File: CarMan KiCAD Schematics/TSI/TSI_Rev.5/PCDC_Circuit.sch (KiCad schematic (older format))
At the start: 56 parts, among them IC1 TS431ILT, J30 GLV Hook-up Pin, K1 APAN3105, Q1 ZVP1320F, Q3 SI1302DL-T1-E3, U10 MC7805BDTRKG, U12 REF3033, U19 SN74HC00APWR, U21 MCP6004, U27 TLP293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

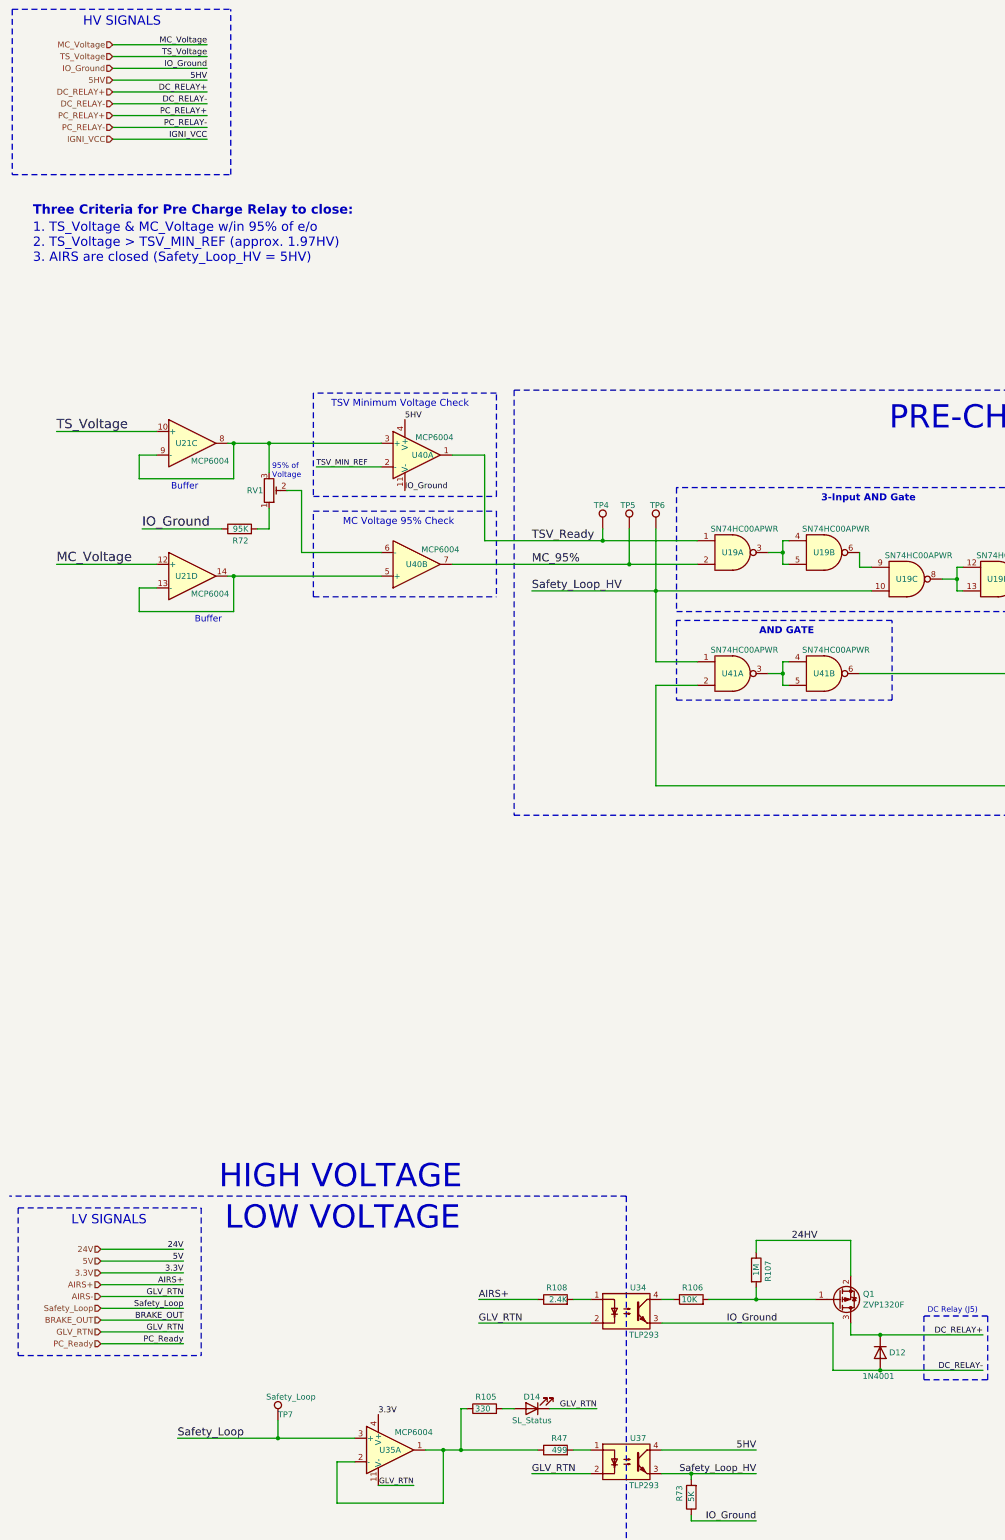
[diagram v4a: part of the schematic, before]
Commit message: General signal directions -> i/o
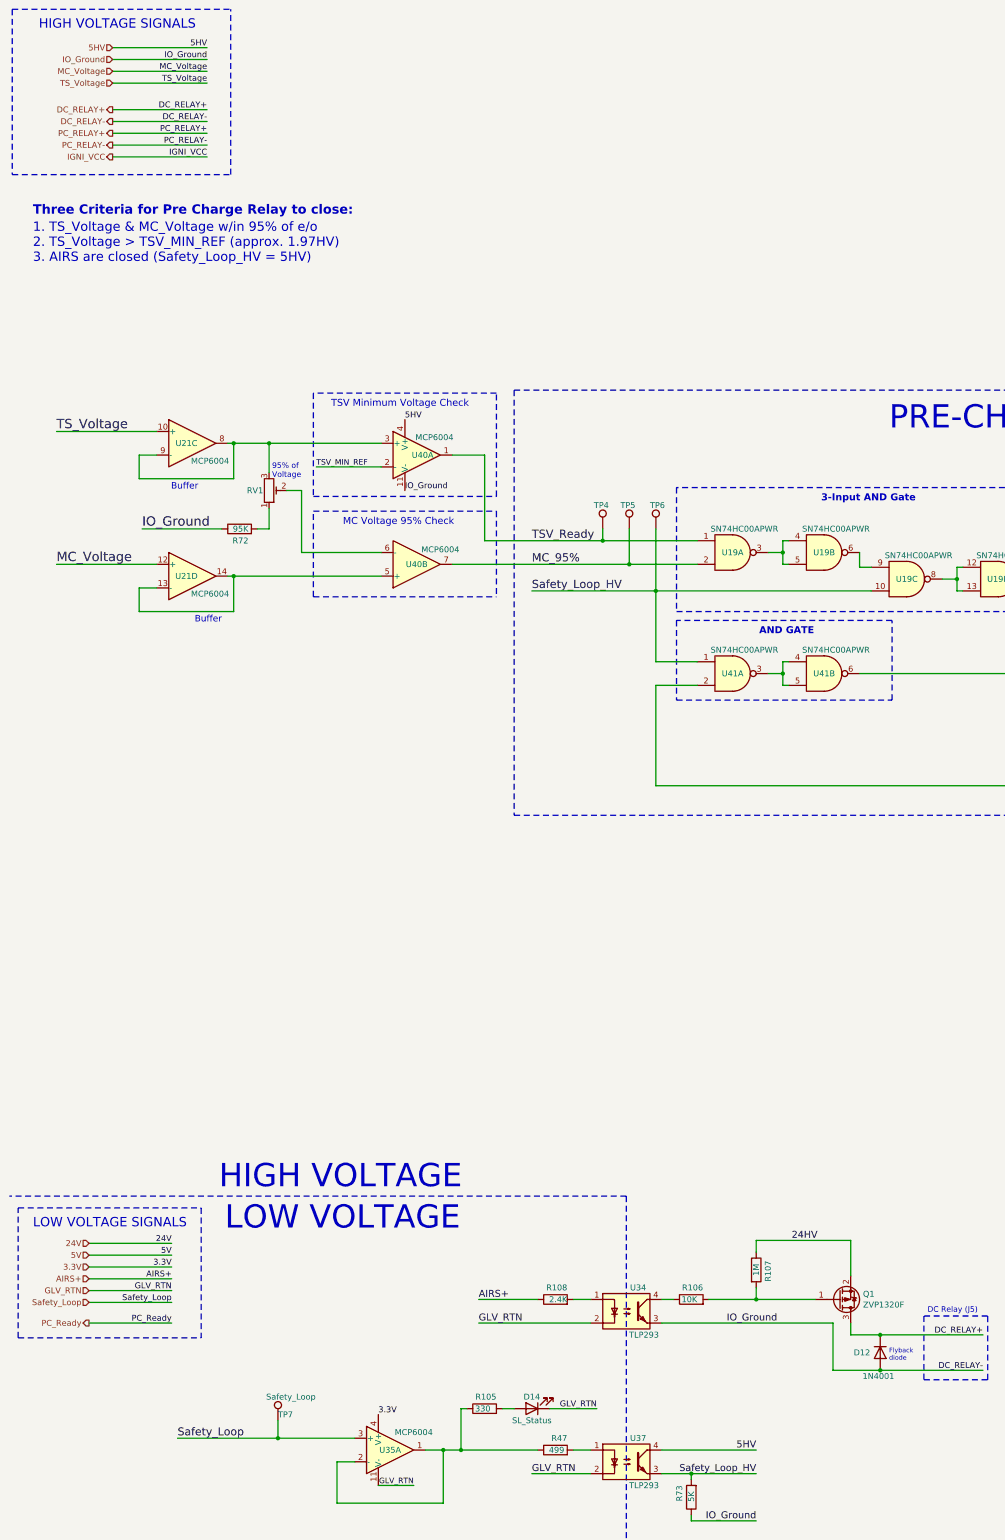
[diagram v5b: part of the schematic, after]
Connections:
- net AIRS- renamed GLV_RTN
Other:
- note added: "Flyback\ndiode"
- note added: "HIGH VOLTAGE SIGNALS\n"
- note added: "LOW VOLTAGE SIGNALS\n"
- note removed: "HV SIGNALS\n"
- note removed: "LV SIGNALS\n"
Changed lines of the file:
@@
 Text Label 21925 1850 2    47   ~ 0
 5HV
-Text Label 2150 800  2    50   ~ 0
+Text Label 2150 1025 2    50   ~ 0
 MC_Voltage
-Text Label 2150 1000 2    50   ~ 0
+Text Label 2150 925  2    50   ~ 0
 IO_Ground
-Text Label 2150 900  2    50   ~ 0
+Text Label 2150 1125 2    50   ~ 0
 TS_Voltage
-Text Notes 1100 650  0    79   ~ 0
-HV SIGNALS\n
-Text HLabel 1350 800  0    50   Input ~ 0
+Text Notes 725  675  0    79   ~ 0
+HIGH VOLTAGE SIGNALS\n
+Text HLabel 1350 1025 0    50   Input ~ 0
 MC_Voltage
 Text Notes 2300 10850 0    197  ~ 0
@@
 U 1 1 6017ACEB
 P 7850 11875
-F 0 "D12" V 7850 11950 50  0000 L CNN
+F 0 "D12" V 7850 11650 50  0000 L CNN
 F 1 "1N4001" V 8050 11725 50  0000 L CNN
 F 2 "Diode_THT:D_DO-41_SOD81_P7.62mm_Horizontal" H 7850 11875 50  0001 C CNN
@@
 Text Notes 13700 4125 0    79   ~ 0
 SR Latching Logic\n
-Text HLabel 1350 900  0    50   Input ~ 0
+Text HLabel 1350 1125 0    50   Input ~ 0
 TS_Voltage
-Text HLabel 1350 1000 0    50   Input ~ 0
+Text HLabel 1350 925  0    50   Input ~ 0
 IO_Ground
-Text Label 2150 1100 2    50   ~ 0
+Text Label 2150 825  2    50   ~ 0
 5HV
-Text HLabel 1350 1100 0    50   Input ~ 0
+Text HLabel 1350 825  0    50   Input ~ 0
 5HV
-Text Label 1950 11700 2    50   ~ 0
+Text Label 1850 11350 2    50   ~ 0
 GLV_RTN
-Text Label 1950 11000 2    50   ~ 0
+Text Label 1850 10950 2    50   ~ 0
 24V
-Text Label 1950 11500 2    50   ~ 0
+Text Label 1850 11450 2    50   ~ 0
 Safety_Loop
-Text Label 1950 11600 2    50   ~ 0
-BRAKE_OUT
-Text Label 1950 11200 2    50   ~ 0
+Text Label 1850 11150 2    50   ~ 0
 3.3V
-Text Label 1950 11100 2    50   ~ 0
+Text Label 1850 11050 2    50   ~ 0
 5V
-Text Notes 1000 10800 0    79   ~ 0
-LV SIGNALS\n
-Text HLabel 1250 11500 0    50   Input ~ 0
+Text Notes 675  10825 0    79   ~ 0
+LOW VOLTAGE SIGNALS\n
+Text HLabel 1150 11450 0    50   Input ~ 0
 Safety_Loop
-Text HLabel 1250 11700 0    50   Input ~ 0
+Text HLabel 1150 11350 0    50   Input ~ 0
 GLV_RTN
-Text HLabel 1250 11000 0    50   Input ~ 0
+Text HLabel 1150 10950 0    50   Input ~ 0
 24V
-Text HLabel 1250 11100 0    50   Input ~ 0
+Text HLabel 1150 11050 0    50   Input ~ 0
 5V
-Text HLabel 1250 11600 0    50   Input ~ 0
-BRAKE_OUT
-Text Label 1950 11400 2    50   ~ 0
-GLV_RTN
-Text Label 1950 11300 2    50   ~ 0
+Text Label 1850 11250 2    50   ~ 0
 AIRS+
-Text HLabel 1250 11400 0    50   Input ~ 0
-AIRS-
-Text HLabel 1250 11300 0    50   Input ~ 0
+Text HLabel 1150 11250 0    50   Input ~ 0
 AIRS+
-Text HLabel 1250 11200 0    50   Input ~ 0
+Text HLabel 1150 11150 0    50   Input ~ 0
 3.3V
 Wire Notes Line
 	550  10650 2100 10650
-Wire Notes Line
-	550  11900 2100 11900
-Text Label 1950 11800 2    50   ~ 0
+Text Label 1850 11625 2    50   ~ 0
 PC_Ready
-Text HLabel 1250 11800 0    50   Input ~ 0
+Text HLabel 1150 11625 0    50   Output ~ 0
 PC_Ready
-Wire Notes Line
-	550  10650 550  11900
-Wire Notes Line
-	2100 10650 2100 11900
 Text Notes 5250 14550 0    47   ~ 0
 24V (GLV) --> 24V (ISO)\n
 Text Notes 19175 15175 0    118  ~ 0
 PRECHARGE & DISCHARGE CIRCUIT
-Text Label 2150 1300 2    50   ~ 0
+Text Label 2150 1450 2    50   ~ 0
 DC_RELAY-
-Text Label 2150 1200 2    50   ~ 0
+Text Label 2150 1350 2    50   ~ 0
 DC_RELAY+
-Text HLabel 1350 1300 0    50   Input ~ 0
+Text HLabel 1350 1450 0    50   Output ~ 0
 DC_RELAY-
-Text HLabel 1350 1200 0    50   Input ~ 0
-DC_RELAY+
-Text Label 2150 1500 2    50   ~ 0
+Text Label 2150 1650 2    50   ~ 0
 PC_RELAY-
-Text Label 2150 1400 2    50   ~ 0
+Text Label 2150 1550 2    50   ~ 0
 PC_RELAY+
-Text HLabel 1350 1500 0    50   Input ~ 0
+Text HLabel 1350 1650 0    50   Output ~ 0
 PC_RELAY-
-Text HLabel 1350 1400 0    50   Input ~ 0
+Text HLabel 1350 1550 0    50   Output ~ 0
 PC_RELAY+
-Text Label 2150 1600 2    50   ~ 0
+Text Label 2150 1750 2    50   ~ 0
 IGNI_VCC
-Text HLabel 1350 1600 0    50   Input ~ 0
+Text HLabel 1350 1750 0    50   Output ~ 0
 IGNI_VCC
 Text Notes 2250 10500 0    197  ~ 0
@@
 	19350 11425 20750 11425
 Wire Wire Line
-	1350 1600 2150 1600
-Wire Wire Line
-	1350 1500 2150 1500
-Wire Wire Line
-	1350 1400 2150 1400
-Wire Wire Line
-	1350 1300 2150 1300
-Wire Wire Line
-	1350 1200 2150 1200
-Wire Wire Line
-	1350 1100 2150 1100
-Wire Wire Line
-	1350 1000 2150 1000
-Wire Wire Line
-	1350 900  2150 900
-Wire Wire Line
-	1350 800  2150 800
-Wire Wire Line
-	1250 11600 1950 11600
-Wire Wire Line
-	1250 11700 1950 11700
-Wire Wire Line
-	1250 11800 1950 11800
-Wire Wire Line
-	1250 11500 1950 11500
-Wire Wire Line
-	1250 11400 1950 11400
-Wire Wire Line
-	1250 11300 1950 11300
-Wire Wire Line
-	1250 11200 1950 11200
-Wire Wire Line
-	1250 11100 1950 11100
-Wire Wire Line
-	1250 11000 1950 11000
+	1350 1750 2150 1750
+Wire Wire Line
+	1350 1650 2150 1650
+Wire Wire Line
+	1350 1550 2150 1550
+Wire Wire Line
+	1350 1450 2150 1450
+Wire Wire Line
+	1350 1350 2150 1350
+Wire Wire Line
+	1350 825  2150 825
+Wire Wire Line
+	1350 925  2150 925
+Wire Wire Line
+	1350 1125 2150 1125
+Wire Wire Line
+	1350 1025 2150 1025
+Wire Wire Line
+	1150 11350 1850 11350
+Wire Wire Line
+	1150 11625 1850 11625
+Wire Wire Line
+	1150 11450 1850 11450
+Wire Wire Line
+	1150 11250 1850 11250
+Wire Wire Line
+	1150 11150 1850 11150
+Wire Wire Line
+	1150 11050 1850 11050
+Wire Wire Line
+	1150 10950 1850 10950
 Text Label 4600 15850 0    59   ~ 0
 5V_ISO_RTN
@@
 P 5100 12700
 F 0 "R47" V 5200 12600 50  0000 L CNN
-F 1 "499" V 5100 12600 50  0000 L CNN
+F 1 "499" V 5100 12625 50  0000 L CNN
 F 2 "Resistor_SMD:R_0805_2012Metric_Pad1.15x1.40mm_HandSolder" V 5030 12700 50  0001 C CNN
 F 3 "~" H 5100 12700 50  0001 C CNN
@@
 Wire Notes Line
 	16725 10400 16725 14650
+Wire Notes Line
+	2100 10650 2100 11750
+Wire Notes Line
+	550  11750 2100 11750
+Wire Notes Line
+	550  11750 550  10650
+Text Notes 7925 11950 0    39   ~ 0
+Flyback\ndiode
+Text HLabel 1350 1350 0    50   Output ~ 0
+DC_RELAY+
 $EndSCHEMATC

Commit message: - Added Test point TSV_MIN_REF - Removed DC_RELAY- signal. changed DC_RELAY- to be IO_Ground instead of IO_Ground shorted to DC_RELAY-, question of net-listing names on board layout more than anything. Was also an attempt to cut down the number of "grounds" there were from GLV_RTN, 5V_ISO_RTN, IO_Ground & DC_RELAY- to just the first three
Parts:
- added TP20: TSV_MIN_REF, TestPoint:TestPoint_Pad_D3.0mm, symbol Connector:TestPoint
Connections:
- net TSV_MIN_REF: now also TP20.1
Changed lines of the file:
@@
 Text Label 4450 11625 0    59   ~ 0
 GLV_RTN
-Text Label 6550 11625 0    59   ~ 0
-IO_Ground
 Text Label 3600 14200 0    59   ~ 0
 GLV_RTN
@@
 Text Label 8720 11725 2    50   ~ 0
 DC_RELAY+
-Text Label 8720 12025 2    50   ~ 0
-DC_RELAY-
 Wire Wire Line
 	7600 11625 7600 11725
@@
 Wire Wire Line
 	7450 11625 7450 12025
-Text Notes 13600 4350 0    79   ~ 0
-~S
-Text Notes 13950 4350 0    79   ~ 0
-~R\n
-Text Notes 14350 4350 0    79   ~ 0
-Q\n
-Wire Bus Line
-	14600 4175 14200 4175
-Wire Bus Line
-	13500 4975 13800 4975
-Wire Bus Line
-	13800 4175 13800 4975
-Connection ~ 13800 4175
-Wire Bus Line
-	13800 4175 13500 4175
-Connection ~ 13800 4975
-Wire Bus Line
-	13800 4975 14200 4975
-Connection ~ 14200 4175
-Wire Bus Line
-	14200 4175 13800 4175
-Text Notes 13600 4500 0    79   ~ 0
-0
-Text Notes 13600 4650 0    79   ~ 0
-0
-Text Notes 13950 4800 0    79   ~ 0
-0
-Text Notes 13950 4500 0    79   ~ 0
-0
-Text Notes 13950 4950 0    79   ~ 0
-1\n
-Text Notes 13600 4800 0    79   ~ 0
-1\n
-Text Notes 13600 4950 0    79   ~ 0
-1\n
-Text Notes 13950 4650 0    79   ~ 0
-1\n
-Text Notes 14350 4650 0    79   ~ 0
-1\n
-Text Notes 14350 4800 0    79   ~ 0
-0
-Connection ~ 14200 4975
-Wire Bus Line
-	14200 4175 14200 4975
-Wire Bus Line
-	14200 4975 14600 4975
-Text Notes 13700 4125 0    79   ~ 0
-SR Latching Logic\n
 Text HLabel 1350 1125 0    50   Input ~ 0
 TS_Voltage
@@
 PRECHARGE & DISCHARGE CIRCUIT
 Text Label 2150 1450 2    50   ~ 0
-DC_RELAY-
+IO_Ground
 Text Label 2150 1350 2    50   ~ 0
 DC_RELAY+
@@
 Text Notes 675  2650 0    79   ~ 0
 1. TS_Voltage & MC_Voltage w/in 95% of e/o\n2. TS_Voltage > TSV_MIN_REF (approx. 1.97HV)\n3. AIRS are closed (Safety_Loop_HV = 5HV)
-Text Label 14600 6625 0    59   ~ 0
-PC_Control
-Wire Wire Line
-	14250 6625 15600 6625
-Connection ~ 14250 6625
-Wire Wire Line
-	13550 6625 14250 6625
 Connection ~ 13550 6625
 Wire Wire Line
@@
 Text Notes 17075 6200 0    35   ~ 0
 Flyback\nDiode
-Wire Wire Line
-	14250 6475 14250 6625
-$Comp
-L Connector:TestPoint TP?
-U 1 1 60D4CBAD
-P 14250 6475
-AR Path="/5FC85F57/60D4CBAD" Ref="TP?"  Part="1"
-AR Path="/6196BF15/60D4CBAD" Ref="TP19"  Part="1"
-F 0 "TP19" H 14200 6675 50  0000 L CNN
-F 1 "PC_Control" H 14275 6525 50  0000 L CNN
-F 2 "TestPoint:TestPoint_Pad_D3.0mm" H 14450 6475 50  0001 C CNN
-F 3 "~" H 14450 6475 50  0001 C CNN
-	1    14250 6475
-	1    0    0    -1
-$EndComp
 Wire Notes Line
 	19425 7325 20775 7325
@@
 Wire Wire Line
 	17500 6325 17500 6425
-Wire Wire Line
-	15100 8375 15600 8375
 Wire Wire Line
 	17500 5625 17500 5775
@@
 Wire Wire Line
 	16600 6425 16500 6425
-$Comp
-L Device:LED D6
-U 1 1 5F9CE834
-P 16600 6225
-F 0 "D6" V 16600 6400 50  0000 R CNN
-F 1 "GREEN LED" H 16825 6050 50  0000 R CNN
-F 2 "LED_SMD:LED_0805_2012Metric_Pad1.15x1.40mm_HandSolder" H 16600 6225 50  0001 C CNN
-F 3 "http://static.vcclite.com/pdf/VAOL-S8GT4-LED-0805-green.pdf" H 16600 6225 50  0001 C CNN
-F 4 "VAOL-S8GT4" V 16600 6225 50  0001 C CNN "Part Name"
-	1    16600 6225
-	0    -1   -1   0
-$EndComp
-$Comp
-L Device:R R67
-U 1 1 5F9DBFC0
-P 16600 5825
-F 0 "R67" V 16500 5825 50  0000 C CNN
-F 1 "2.4K" V 16600 5825 50  0000 C CNN
-F 2 "Resistor_SMD:R_0805_2012Metric_Pad1.15x1.40mm_HandSolder" V 16530 5825 50  0001 C CNN
-F 3 "~" H 16600 5825 50  0001 C CNN
-	1    16600 5825
-	-1   0    0    1
-$EndComp
 Wire Wire Line
 	16600 5625 16600 5675
@@
 Text Label 16300 5625 0    50   ~ 0
 24HV
-Text Label 15100 8375 0    55   ~ 0
-IO_Ground
 Wire Wire Line
 	15600 8375 15600 8175
@@
 Wire Wire Line
 	19700 3400 19950 3400
-Text Notes 14750 4350 0    79   ~ 0
-~Q\n
-Wire Bus Line
-	15000 4175 14600 4175
-Text Notes 14750 4800 0    79   ~ 0
-1
-Text Notes 14750 4950 0    79   ~ 0
-X
-Text Notes 14750 4500 0    79   ~ 0
-X
-Connection ~ 14600 4175
-Connection ~ 14600 4975
-Wire Bus Line
-	14600 4175 14600 4975
-Wire Bus Line
-	14600 4975 15000 4975
-Wire Bus Line
-	15000 4375 13500 4375
-Wire Notes Line
-	13500 4525 15000 4525
-Wire Notes Line
-	13500 4675 15000 4675
-Wire Notes Line
-	13500 4825 15000 4825
-Text Notes 14425 4500 2    79   ~ 0
-X
-Text Notes 14350 4950 0    79   ~ 0
-X
-Text Notes 14750 4650 0    79   ~ 0
-0\n
-Connection ~ 13500 4375
-Wire Bus Line
-	13500 4375 13500 4975
-Connection ~ 15000 4375
-Wire Bus Line
-	15000 4375 15000 4975
-Wire Bus Line
-	13500 4175 13500 4375
-Wire Bus Line
-	15000 4175 15000 4375
 $Comp
 L Connector:TestPoint TP?
@@
 	4750 3725 4750 7325
 Wire Notes Line
-	4750 3725 15250 3725
-Wire Notes Line
-	4750 7325 15250 7325
-Wire Notes Line
-	15250 3725 15250 7325
-Wire Notes Line
 	18075 3600 22100 3600
 Wire Notes Line
@@
 Text HLabel 1350 1350 0    50   Output ~ 0
 DC_RELAY+
+$Comp
+L Connector:TestPoint TP?
+U 1 1 64A39D43
+P 19350 11275
+AR Path="/5FC85F57/64A39D43" Ref="TP?"  Part="1"
+AR Path="/6196BF15/64A39D43" Ref="TP20"  Part="1"
+F 0 "TP20" H 19300 11475 50  0000 L CNN
+F 1 "TSV_MIN_REF" H 19125 11550 50  0001 L CNN
+F 2 "TestPoint:TestPoint_Pad_D3.0mm" H 19550 11275 50  0001 C CNN
+F 3 "~" H 19550 11275 50  0001 C CNN
+	1    19350 11275
+	1    0    0    -1
+$EndComp
+Text Label 15100 8375 0    55   ~ 0
+IO_Ground
+Wire Wire Line
+	15100 8375 15600 8375
+$Comp
+L Device:LED D6
+U 1 1 5F9CE834
+P 16600 6225
+F 0 "D6" V 16600 6400 50  0000 R CNN
+F 1 "GREEN LED" H 16825 6050 50  0000 R CNN
+F 2 "LED_SMD:LED_0805_2012Metric_Pad1.15x1.40mm_HandSolder" H 16600 6225 50  0001 C CNN
+F 3 "http://static.vcclite.com/pdf/VAOL-S8GT4-LED-0805-green.pdf" H 16600 6225 50  0001 C CNN
+F 4 "VAOL-S8GT4" V 16600 6225 50  0001 C CNN "Part Name"
+	1    16600 6225
+	0    -1   -1   0
+$EndComp
+Wire Notes Line
+	4750 3725 15250 3725
+Wire Notes Line
+	4750 7325 15250 7325
+Text Label 14600 6625 0    59   ~ 0
+PC_Control
+Connection ~ 14250 6625
+Wire Wire Line
+	14250 6625 15600 6625
+Wire Wire Line
+	13550 6625 14250 6625
+$Comp
+L Connector:TestPoint TP?
+U 1 1 60D4CBAD
+P 14250 6475
+AR Path="/5FC85F57/60D4CBAD" Ref="TP?"  Part="1"
+AR Path="/6196BF15/60D4CBAD" Ref="TP19"  Part="1"
+F 0 "TP19" H 14200 6675 50  0000 L CNN
+F 1 "PC_Control" H 14275 6525 50  0000 L CNN
+F 2 "TestPoint:TestPoint_Pad_D3.0mm" H 14450 6475 50  0001 C CNN
+F 3 "~" H 14450 6475 50  0001 C CNN
+	1    14250 6475
+	1    0    0    -1
+$EndComp
+Wire Wire Line
+	14250 6475 14250 6625
+Wire Notes Line
+	15250 3725 15250 7325
+Wire Bus Line
+	15000 4175 15000 4375
+Wire Bus Line
+	13500 4175 13500 4375
+Wire Bus Line
+	15000 4375 15000 4975
+Connection ~ 15000 4375
+Wire Bus Line
+	13500 4375 13500 4975
+Connection ~ 13500 4375
+Text Notes 14750 4650 0    79   ~ 0
+0\n
+Text Notes 14350 4950 0    79   ~ 0
+X
+Text Notes 14425 4500 2    79   ~ 0
+X
+Wire Notes Line
+	13500 4825 15000 4825
+Wire Notes Line
+	13500 4675 15000 4675
+Wire Notes Line
+	13500 4525 15000 4525
+Wire Bus Line
+	15000 4375 13500 4375
+Wire Bus Line
+	14600 4975 15000 4975
+Wire Bus Line
+	14600 4175 14600 4975
+Connection ~ 14600 4975
+Connection ~ 14600 4175
+Text Notes 14750 4500 0    79   ~ 0
+X
+Text Notes 14750 4950 0    79   ~ 0
+X
+Text Notes 14750 4800 0    79   ~ 0
+1
+Wire Bus Line
+	15000 4175 14600 4175
+Text Notes 14750 4350 0    79   ~ 0
+~Q\n
+Text Notes 13700 4125 0    79   ~ 0
+SR Latching Logic\n
+Wire Bus Line
+	14200 4975 14600 4975
+Wire Bus Line
+	14200 4175 14200 4975
+Connection ~ 14200 4975
+Text Notes 14350 4800 0    79   ~ 0
+0
+Text Notes 14350 4650 0    79   ~ 0
+1\n
+Text Notes 13950 4650 0    79   ~ 0
+1\n
+Text Notes 13600 4950 0    79   ~ 0
+1\n
+Text Notes 13600 4800 0    79   ~ 0
+1\n
+Text Notes 13950 4950 0    79   ~ 0
+1\n
+Text Notes 13950 4500 0    79   ~ 0
+0
+Text Notes 13950 4800 0    79   ~ 0
+0
+Text Notes 13600 4650 0    79   ~ 0
+0
+Text Notes 13600 4500 0    79   ~ 0
+0
+Wire Bus Line
+	14200 4175 13800 4175
+Connection ~ 14200 4175
+Wire Bus Line
+	13800 4975 14200 4975
+Connection ~ 13800 4975
+Wire Bus Line
+	13800 4175 13500 4175
+Connection ~ 13800 4175
+Wire Bus Line
+	13800 4175 13800 4975
+Wire Bus Line
+	13500 4975 13800 4975
+Wire Bus Line
+	14600 4175 14200 4175
+Text Notes 14350 4350 0    79   ~ 0
+Q\n
+Text Notes 13950 4350 0    79   ~ 0
+~R\n
+Text Notes 13600 4350 0    79   ~ 0
+~S
+$Comp
+L Device:R R67
+U 1 1 5F9DBFC0
+P 16600 5825
+F 0 "R67" V 16500 5825 50  0000 C CNN
+F 1 "2.4K" V 16600 5825 50  0000 C CNN
+F 2 "Resistor_SMD:R_0805_2012Metric_Pad1.15x1.40mm_HandSolder" V 16530 5825 50  0001 C CNN
+F 3 "~" H 16600 5825 50  0001 C CNN
+	1    16600 5825
+	-1   0    0    1
+$EndComp
+Text Label 8720 12025 2    50   ~ 0
+IO_Ground
 $EndSCHEMATC
